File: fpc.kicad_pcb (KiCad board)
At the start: 2 copper layers, 251.1 x 145.4 mm, 88 parts, among them J16 Screw_Terminal_01x04, J17 Screw_Terminal_01x04, J18 Screw_Terminal_01x04, J19 Screw_Terminal_01x04, J20 Screw_Terminal_01x04, J21 Screw_Terminal_01x04, J22 15v, J3 Screw_Terminal_01x04, J4 Screw_Terminal_01x04, J5 Conn_01x02_Socket, J6 Conn_01x16_Socket, J7 Conn_01x16_Socket, K1 Relay_SPDT, K2 Relay_SPDT, K3 Relay_SPDT, K4 Relay_SPDT, Q1 BC547, Q6 BC547, Q7 BC547, Q8 BC547, U5 ESP32-S3-DEVKITC-1U-N8R8, U6 RS485_TTL_Module, U7 ZC261500

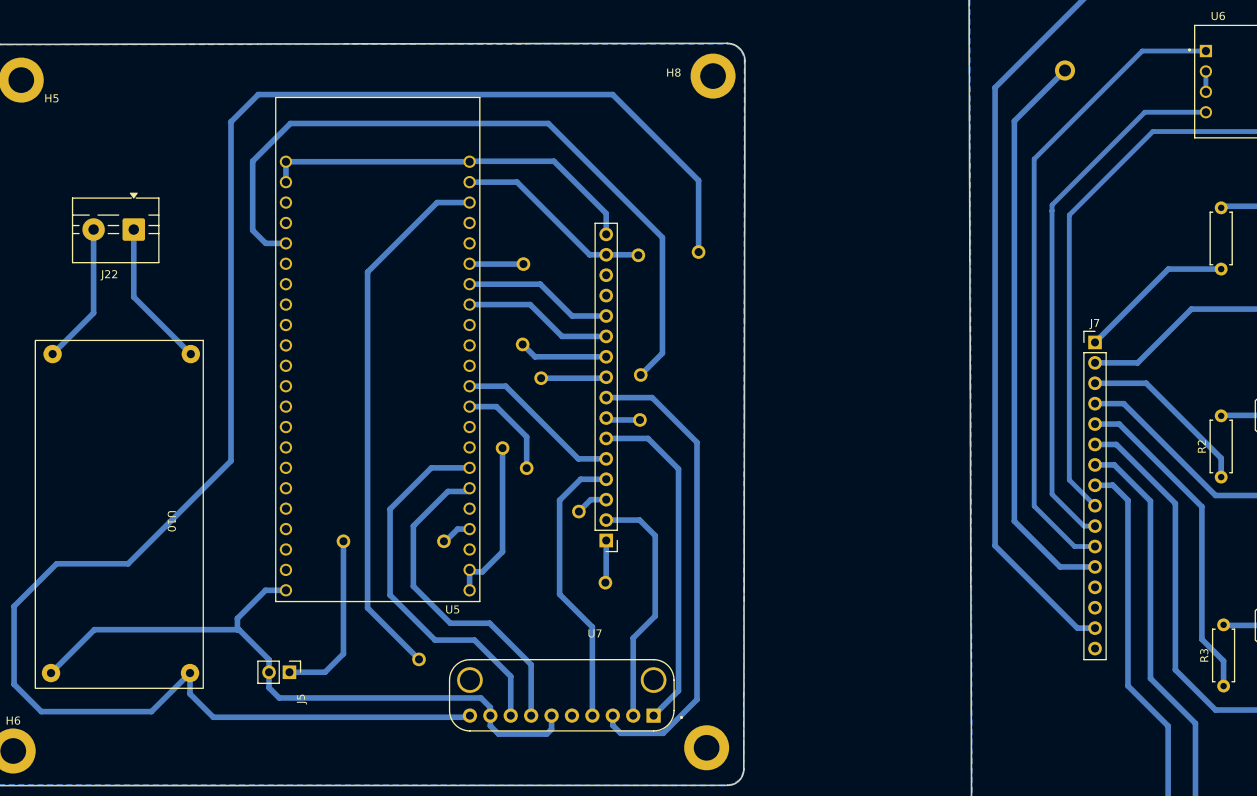
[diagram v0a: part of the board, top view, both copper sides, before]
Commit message: Remove unnecessary local files - Change the label name for the pins - Reroute the relay part of the board
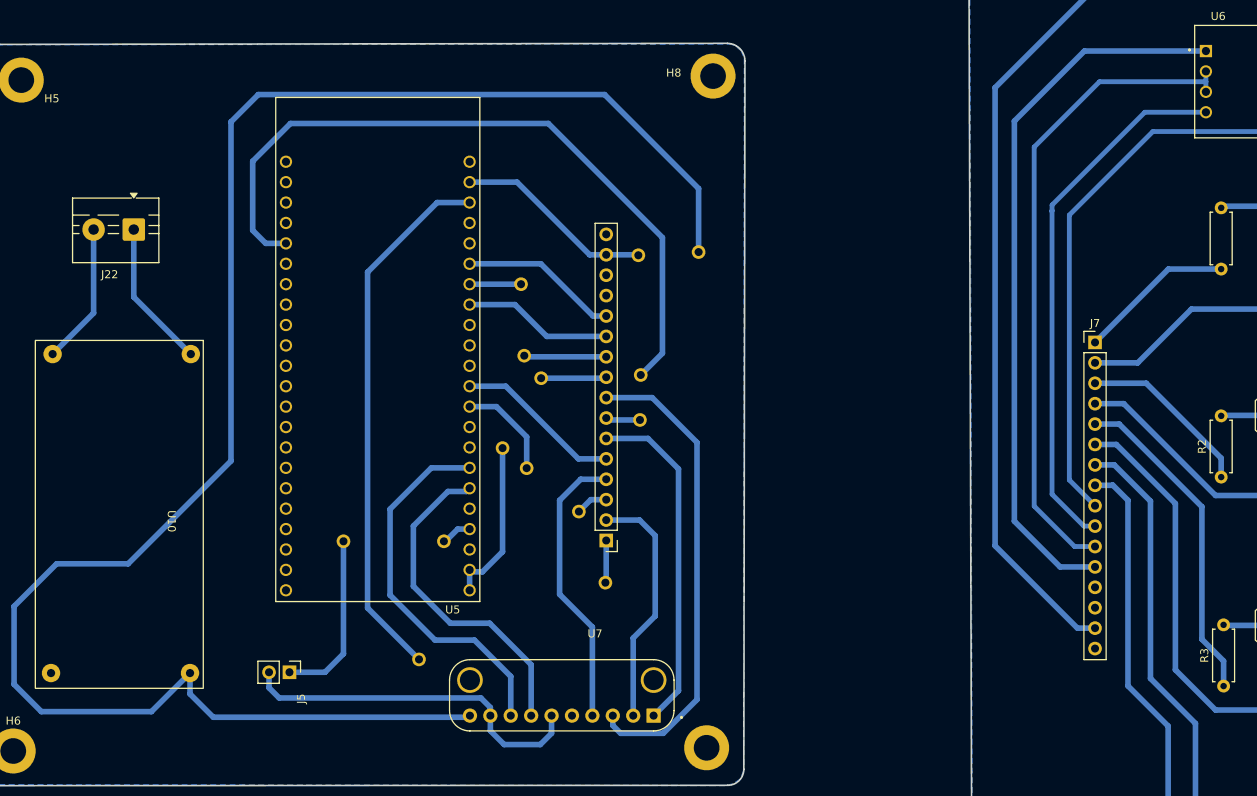
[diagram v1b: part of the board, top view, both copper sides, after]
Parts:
- removed the ? at (155.7, 131.2)
- removed the ? at (223.2, 97.1)
- added ?: , , F.Cu at (155.5, 123.7)
- moved ? 11.4 mm to (155.9, 132.6)
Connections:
- net /1AC+ renamed /Power_Source_1
- net /3AC+ renamed /Power_Source_3
- net /4AC+ renamed /Power_Source_4
- net Net-(J18-Pin_2) renamed /Neutral_1
- net Net-(J19-Pin_2) renamed /Neutral_2
- net Net-(J20-Pin_2) renamed /Neutral_3
- net Net-(J21-Pin_2) renamed /Neutral_4
- ? pad 18: /RX_PIN -> /TX_PIN
- J19 pad 4: /2AC+ -> /Power_Source_2
- J6 pad 1: /GPIO14 -> /RELAY_1
- J6 pad 10: /RX_PIN -> /TX_PIN
- J6 pad 12: /TX_PIN -> /RX_PIN
- J6 pad 2: /A2+ -> /Curr_analog_out3
- J6 pad 3: /GPIO17 -> /RELAY_2
- J6 pad 4: /A0+ -> /Curr_analog_out1
- J6 pad 5: /GPIO18 -> /RELAY_3
- J6 pad 6: /A3+ -> /Curr_analog_out4
- J6 pad 7: /GPIO21 -> /RELAY_4
- J6 pad 8: /A1+ -> /Curr_analog_out2
- J7 pad 10: /RX_PIN -> /TX_PIN
- J7 pad 12: /TX_PIN -> /RX_PIN
- J7 pad 2: /A2 -> /Curr_analog_out3
- J7 pad 4: /A0 -> /Curr_analog_out1
- J7 pad 6: /A3 -> /Curr_analog_out4
- J7 pad 8: /A1 -> /Curr_analog_out2
- K4 pad 1: unconnected-(K4-Pad1) -> /Power_Source_2
- U1 pad 2: /A0 -> /Curr_analog_out1
- U2 pad 2: /A2 -> /Curr_analog_out3
- U3 pad 2: /A1 -> /Curr_analog_out2
- U4 pad 2: /A3 -> /Curr_analog_out4
- U5 pad J1_10: /GPIO17 -> /RELAY_2
- U5 pad J1_11: /GPIO18 -> /RELAY_3
- U5 pad J1_20: /GPIO14 -> /RELAY_1
- U5 pad J3_18: /GPIO21 -> /RELAY_4
- U7 pad 1: /A3+ -> /Curr_analog_out4
- U7 pad 2: /A2+ -> /Curr_analog_out3
- U7 pad 3: /A1+ -> /Curr_analog_out2
- U7 pad 4: /A0+ -> /Curr_analog_out1
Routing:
- net (no net): track 146.8 -> 0.00 mm
- net /Curr_analog_out2: track 0.00 -> 144.8 mm
- net /Curr_analog_out4: track 0.00 -> 106.6 mm
- net /RX_PIN: track 17.8 -> 109.4 mm
- net GND: track 312.8 -> 225.5 mm
- net /A1: track 85.3 -> 0.00 mm
- net /DRI: track 21.2 -> 100.3 mm
- net /Curr_analog_out1: track 0.00 -> 77.8 mm
- net /Curr_analog_out3: track 0.00 -> 74.6 mm
- net /RE: track 71.1 -> 0.00 mm
- net /TX_PIN: track 18.6 -> 83.7 mm
- net /A3: track 64.0 -> 0.00 mm
- net /A1+: track 59.5 -> 0.00 mm
- net /A2: track 43.7 -> 0.00 mm
- net /A3+: track 42.6 -> 0.00 mm
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
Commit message: Reviewed schematics and PCB before fabrication
- Updated schematics track names
- PCB: rerouted tracks and fix violations
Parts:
- removed the ? at (316.6, 103.1)
- removed the ? at (316.5, 119.7)
- removed the ? at (317.5, 197.9)
- added ?: , , F.Cu at (230.1, 193.9)
- added ?: , , F.Cu at (317.6, 197.0)
- added ?: , , F.Cu at (290.6, 126.9)
- added ?: , , F.Cu at (215.8, 193.9)
- added J1: Screw_Terminal_01x02, TerminalBlock:TerminalBlock_Xinya_XY308-2.54-2P_1x02_P2.54mm_Horizontal, F.Cu at (181.4, 137.1)
- R1, R2, R3, R4: value 1k -> 220R
- U10: value ~ -> BUCK CONVERTER
- moved J22 15.9 mm to (91.5, 115.6), turned to -90 degrees
- moved ? 6.35 mm to (167.1, 167.1)
- moved ? 5.40 mm to (156.2, 152.0)
- moved ? 5.10 mm to (153.0, 134.4)
- moved ? 4.20 mm to (140.2, 167.1)
- moved U10 3.20 mm to (103.0, 153.2)
- moved ? 2.72 mm to (170.1, 132.3)
- moved ? 2.35 mm to (155.4, 130.3)
- moved ? 1.40 mm to (269.5, 126.3)
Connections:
- net /-1PUMP+ renamed /PUMP1_OUT
- net /-2PUMP+ renamed /PUMP2_OUT
- net /-3PUMP+ renamed /PUMP3_OUT
- net /-4PUMP+ renamed /PUMP4_OUT
- net /1PUMP+ renamed /PUMP1_IN
- net /2 renamed /RS485_B
- net /2PUMP+ renamed /PUMP2_IN
- net /3 renamed /RS485_A
- net /3PUMP+ renamed /PUMP3_IN
- net /4PUMP+ renamed /PUMP4_IN
- net /GPIO4 renamed /CHANGE_MODE_BTN
- net Net-(J22-Pin_1) renamed /PWR_IN+
- ? pad 5: VCC -> +5V (x8)
- ? pad 14: /GPIO14 -> /RELAY_1 (x2)
- ? pad 20: /GPIO21 -> /RELAY_4 (x2)
- ? pad 15: /GPIO17 -> /RELAY_2 (x2)
- IN1 pad 1: VCC -> +5V
- IN6 pad 1: VCC -> +5V
- IN7 pad 1: VCC -> +5V
- IN8 pad 1: VCC -> +5V
- J16 pad 1: VCC -> /SENSOR_SUPPLY_3+
- J17 pad 1: VCC -> /SENSOR_SUPPLY_4+
- J22 pad 2: Net-(J22-Pin_2) -> GND
- J3 pad 1: VCC -> /SENSOR_SUPPLY_1+
- J4 pad 1: VCC -> /SENSOR_SUPPLY_2+
- J7 pad 15: VCC -> +5V
- J7 pad 9: +3.3V -> 3.3V
- K1 pad 5: VCC -> +5V
- K2 pad 5: VCC -> +5V
- K3 pad 5: VCC -> +5V
- K4 pad 5: VCC -> +5V
- U1 pad 3: VCC -> +5V
- U10 pad 2: Net-(J22-Pin_2) -> GND
- U2 pad 3: VCC -> +5V
- U3 pad 3: VCC -> +5V
- U4 pad 3: VCC -> +5V
- U6 pad 8: +3.3V -> 3.3V
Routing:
- net +5V: track 247.3 -> 611.4 mm
- net VCC: track 356.9 -> 0.00 mm
- net 3.3V: track 28.8 -> 164.2 mm
- net +3.3V: track 104.2 -> 0.00 mm
- net /RELAY_1: track 19.5 -> 121.8 mm
- net /RELAY_4: track 61.0 -> 161.6 mm
- net /GPIO21: track 94.8 -> 0.00 mm
- net /GPIO14: track 72.6 -> 0.00 mm
- net Net-(IN6-A): track 22.8 -> 68.2 mm
- net Net-(IN8-A): track 27.3 -> 67.6 mm
- net Net-(IN1-A): track 28.7 -> 68.0 mm
- net Net-(IN7-A): track 28.2 -> 67.1 mm
- net GND: track 225.5 -> 259.4 mm
- net /RELAY_2: track 21.9 -> 50.4 mm
- net Net-(J22-Pin_2): track 17.6 -> 0.00 mm
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
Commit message: Update PCB layout and schematic
- Change esp32s3 footprint.
- Add 3D model for esp32s3 footprint.
- Update schematic with new footprint.
- Update pads for the footprint to suite local PCB fab.
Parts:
- removed the ? at (270.3, 185.6)
- removed the ? at (309.7, 107.6)
- removed the ? at (252.7, 155.3)
- removed the ? at (230.1, 193.9)
- removed the ? at (272.8, 83.0)
- removed the ? at (265.8, 108.0)
- removed the ? at (285.2, 102.0)
- removed the ? at (289.9, 85.4)
- removed the ? at (294.9, 88.7)
- removed the ? at (294.8, 82.8)
- removed the ? at (252.7, 133.2)
- removed the ? at (317.6, 197.0)
- removed the ? at (317.0, 146.5)
- removed the ? at (290.0, 93.5)
- removed the ? at (252.7, 181.7)
- removed the ? at (275.9, 107.1)
- removed the ? at (309.9, 133.9)
- removed the ? at (250.9, 88.9)
- removed the ? at (253.2, 205.3)
- removed the ? at (272.9, 88.7)
- removed the ? at (316.5, 123.6)
- removed the ? at (250.9, 83.1)
- removed the ? at (290.6, 126.9)
- removed the ? at (310.5, 185.5)
- removed the ? at (317.1, 172.9)
- removed the ? at (269.5, 126.3)
- removed the ? at (271.1, 133.6)
- removed the ? at (270.7, 159.2)
- removed the ? at (215.8, 193.9)
- removed the ? at (309.9, 159.4)
- removed U5: ESP32-S3-DEVKITC-1U-N8R8, RF_Module:MODULE_ESP32-S3-DEVKITC-1U-N8R8
- added ?: , , F.Cu at (334.3, 152.7)
- added ?: , , F.Cu at (270.0, 161.5)
- added ?: , , F.Cu at (268.2, 95.1)
- added ?: , , F.Cu at (290.2, 94.9)
- added ?: , , F.Cu at (333.8, 129.8)
- added ?: , , F.Cu at (270.0, 139.4)
- added ?: , , F.Cu at (283.1, 114.2)
- added ?: , , F.Cu at (286.8, 132.5)
- added ?: , , F.Cu at (270.5, 211.5)
- added ?: , , F.Cu at (270.0, 187.9)
- added ?: , , F.Cu at (288.4, 139.8)
- added ?: , , F.Cu at (233.1, 200.1)
- added ?: , , F.Cu at (327.2, 165.6)
- added ?: , , F.Cu at (327.8, 191.7)
- added ?: , , F.Cu at (334.9, 203.2)
- added ?: , , F.Cu at (334.4, 179.1)
- added ?: , , F.Cu at (327.0, 113.8)
- added ?: , , F.Cu at (312.1, 89.0)
- added ?: , , F.Cu at (307.2, 91.6)
- added ?: , , F.Cu at (288.0, 165.4)
- added ?: , , F.Cu at (307.3, 99.7)
- added ?: , , F.Cu at (327.2, 140.1)
- added ?: , , F.Cu at (247.4, 200.1)
- added ?: , , F.Cu at (287.6, 191.8)
- added ?: , , F.Cu at (290.1, 89.2)
- added ?: , , F.Cu at (302.5, 108.2)
- added ?: , , F.Cu at (268.2, 89.3)
- added ?: , , F.Cu at (293.2, 113.3)
- added ?: , , F.Cu at (307.9, 133.1)
- added ?: , , F.Cu at (312.2, 94.9)
- added U8: ESP32-S3-DEVKIT-LIPO, footprints:XCVR_ESP32-S3-DEVKIT-LIPO, F.Cu at (136.6, 135.0)
- moved IN1 18.4 mm to (272.8, 181.6)
- moved H1 18.4 mm to (232.8, 214.8)
- moved H2 18.4 mm to (232.6, 77.9)
- moved H3 18.4 mm to (352.5, 77.5)
- moved H4 18.4 mm to (352.4, 214.1)
- moved IN6 18.4 mm to (273.3, 128.9)
- moved IN7 18.4 mm to (272.9, 155.1)
- moved J16 18.4 mm to (322.1, 82.7)
- moved J17 18.4 mm to (344.2, 82.9)
- moved J18 18.4 mm to (341.9, 157.1)
- moved J19 18.4 mm to (342.4, 209.5)
- moved J20 18.4 mm to (341.5, 131.1)
- moved J21 18.4 mm to (342.2, 182.8)
- moved J3 18.4 mm to (278.2, 82.9)
- moved J4 18.4 mm to (300.1, 82.9)
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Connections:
- J17 pad 1: /SENSOR_SUPPLY_4+ -> /SENSOR_SUPPLY_3+
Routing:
- net /RELAY_4: track 161.6 -> 164.5 mm
- net /RS485_B: track 158.5 -> 159.8 mm
- net /SDA: track 41.5 -> 42.3 mm
- net /SENSOR_SUPPLY_4+: track 0.70 -> 0.00 mm
- net /SENSOR_SUPPLY_3+: track 0.00 -> 0.70 mm
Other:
- board size 251.1 x 145.4 mm -> 268.4 x 145.4 mm
